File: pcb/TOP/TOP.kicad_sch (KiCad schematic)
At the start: 90 parts, among them J1 Conn_01x04, Q1 BF545A, Q2 BF545A, U1 ICL7660, U2 L78L15_SOT89, U3 TL074, U4 OPA2604

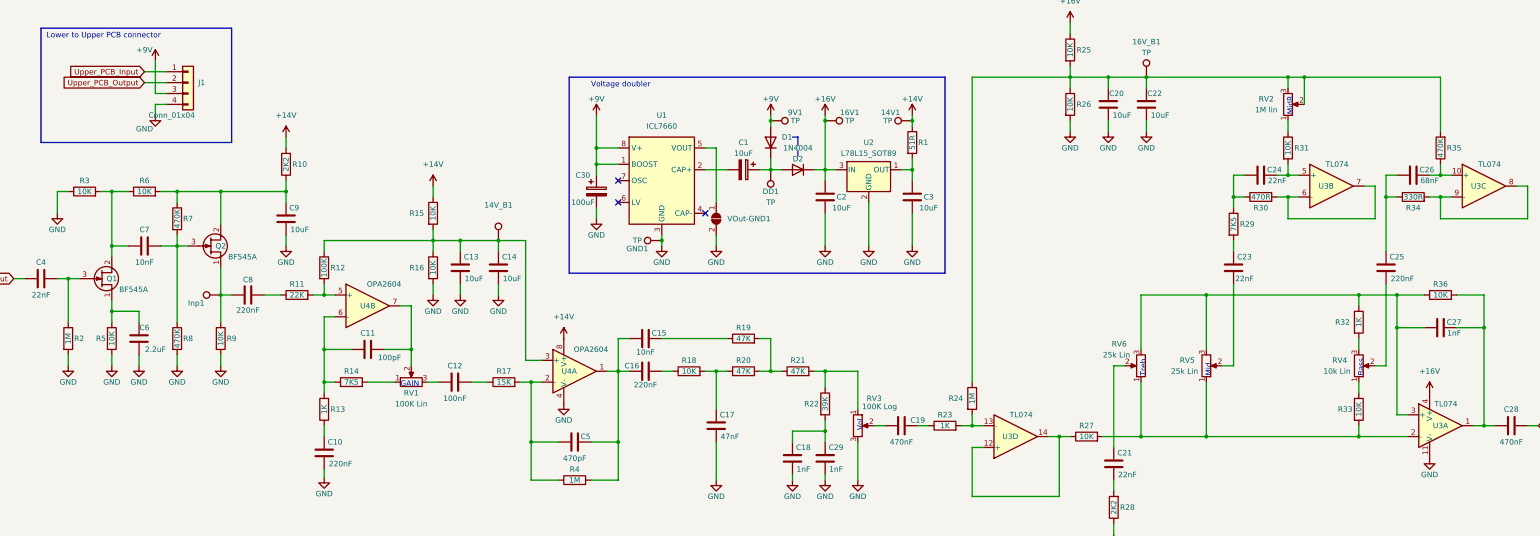
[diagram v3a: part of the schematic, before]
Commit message: [TOP] Fix various problems of first design:
- Some pins of TL072 swapped
- Volume pot inverted
- BOOST input of 7660 now only settable via jumper
- Add option of TO-92/BF245 instead of SOT-23/BF545
-
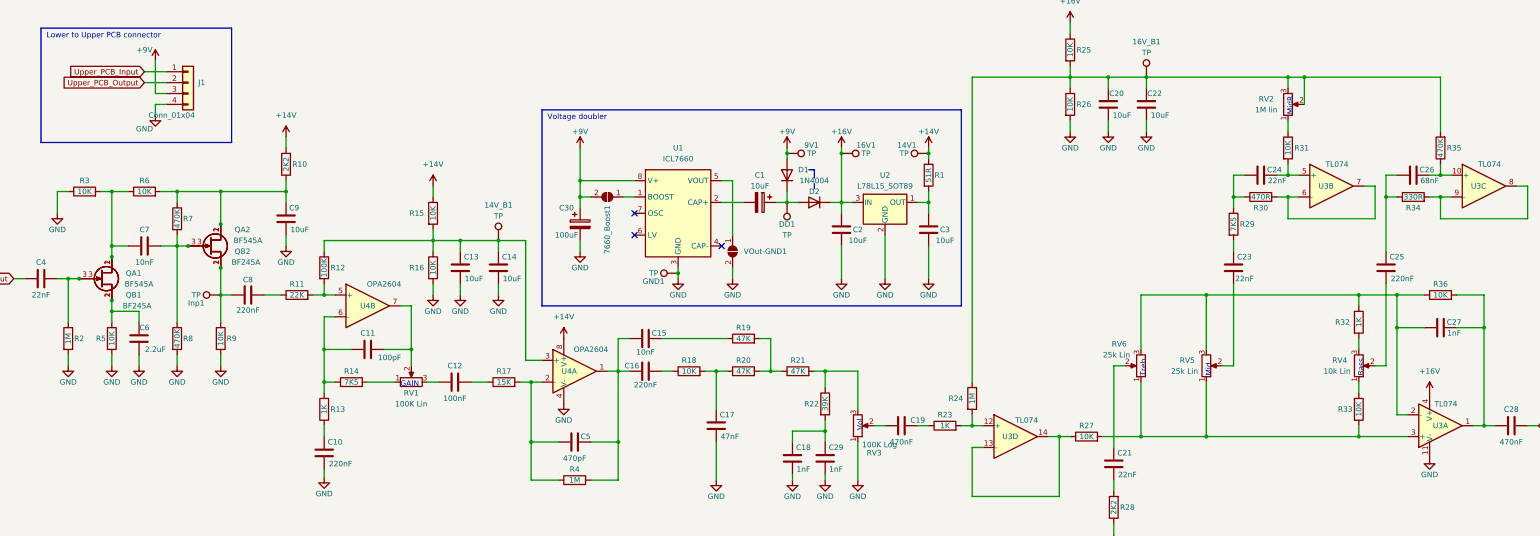
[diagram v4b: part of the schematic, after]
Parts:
- added 7660_Boost1: Jmp, Jumper:SolderJumper-2_P1.3mm_Open_TrianglePad1.0x1.5mm, symbol Jumper:SolderJumper_2_Open
- added QB1, QB2: BF245A, Package_TO_SOT_THT:TO-92L_Inline, symbol Device:Q_NJFET_DSG
- 14V_B1, Inp1: value (none) -> TP; footprint (none) -> TestPoint:TestPoint_Pad_D2.0mm
- renumbered Q1 to QA1, Q2 to QA2
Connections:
- net +9V: now also 7660_Boost1.2 (B); no longer U1.1 (BOOST)
- net GND: now also RV3.1; no longer RV3.3
- net at C9.1, QA2.2 (D), R10.1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: now also QB2.1 (D)
- net at C7.1, QA2.3 (G), R7.2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: now also QB2.3 (G)
- net at C8.2, Inp1.1, QA2.1 (S)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: now also QB2.2 (S)
- net at R27.2, R33.2, RV5.1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: now also U3.3 (+); no longer U3.2 (-)
- net at C27.2, R32.1, R36.1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: now also U3.2 (-); no longer U3.3 (+)
- net at R23.2, R24.2: now also U3.12 (+); no longer U3.13 (-)
- net at R27.1, U3.14: now also U3.13 (-); no longer U3.12 (+)
- net at C6.1, QA1.1 (S), R5.1: now also QB1.2 (S)
- net at C7.2, QA1.2 (D), R3.2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: now also QB1.1 (D)
- net at C4.1, QA1.3 (G), R2.1: now also QB1.3 (G)
- net at R21.2, R22.1: now also RV3.3; no longer RV3.1
- new net: 7660_Boost1.1 (A), U1.1 (BOOST)
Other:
- moved on the sheet: 14V1, 16V1, 9V1, C1, C2, C3, C30, D1, D2, DD1, GND1, R1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
